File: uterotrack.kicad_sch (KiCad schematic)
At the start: 0 parts

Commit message: Add schematics
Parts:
- added AE?: Antenna_Shield, myDevices:SMD_PAD_4x1.5mm, symbol Device:Antenna
- added C? (x2): C, Capacitor_SMD:C_0402_1005Metric, symbol Device:C
- added C? (x5): 100nF, Capacitor_SMD:C_0603_1608Metric, symbol Device:C
- added C? (x2): 10uF, Capacitor_SMD:C_0603_1608Metric, symbol Device:C
- added C?: 1uF, Capacitor_SMD:C_0603_1608Metric, symbol Device:C
- added C?: 10nF, Capacitor_SMD:C_0603_1608Metric, symbol Device:C
- added D?: QLS6B-FKW, LED_SMD:LED_Cree-PLCC6_4.7x1.5mm, symbol LED:QLS6B-FKW
- added J?: RFShield, myDevices:Wuerth_36103255S_25x25mm, symbol Device:RFShield_OnePiece
- added J?: Argos_Prog, Connector_Molex:Molex_PicoBlade_53047-0510_1x05_P1.25mm_Vertical, symbol Connector_Generic:Conn_01x05
- added J?: MicroSD_Card, myDevices:microSD, symbol myDevices:Micro_SD_Card
- added J?: EXP, Connector_PinHeader_2.54mm:PinHeader_1x02_P2.54mm_Vertical, symbol Connector_Generic:Conn_01x02
- added J?: Prog, Connector_Molex:Molex_PicoBlade_53047-0510_1x05_P1.25mm_Vertical, symbol Connector_Generic:Conn_01x05
- added JP?: SolderJumper_3_Open, Jumper:SolderJumper-3_P1.3mm_Open_RoundedPad1.0x1.5mm, symbol Jumper:SolderJumper_3_Open
- added L?: L, Inductor_SMD:L_0603_1608Metric, symbol Device:L
- added Q? (x3): MMBT2222, Package_TO_SOT_SMD:SOT-323_SC-70, symbol Transistor_BJT:Q_NPN_BEC
- added Q?: SiS415DNT, Package_SO:Vishay_PowerPAK_1212-8_Single, symbol Transistor_FET:SiS415DNT
- added Q? (x4): SI2305, Package_TO_SOT_SMD:SOT-23, symbol Transistor_FET:Q_PMOS_GSD
- added Q? (x3): MMBT2222, Package_TO_SOT_SMD:SOT-23, symbol Transistor_BJT:Q_NPN_BEC
- added R? (x9): 10k, Resistor_SMD:R_0603_1608Metric, symbol Device:R
- added R? (x12): 100k, Resistor_SMD:R_0603_1608Metric, symbol Device:R
- added R? (x2): 20k, Resistor_SMD:R_0603_1608Metric, symbol Device:R
- added R? (x6): 0R, Resistor_SMD:R_0603_1608Metric, symbol Device:R
- added R? (x3): 4k7, Resistor_SMD:R_0603_1608Metric, symbol Device:R
- added RN? (x4): 470R, Resistor_SMD:R_Array_Convex_4x0603, symbol Device:R_Pack04_Split
- added U?: RV-3032-C7, myDevices:RTC_SMD_MicroCrystal_C7_1.5x3.2mm, symbol myDevices:RV-3032-C7
- added U?: Argos_SMD, myDevices:Argos-SMD_shortLegs, symbol myDevices:Argos_SMD
- added U?: ESP32-S3-WROOM-1, RF_Module:ESP32-S3-WROOM-1, symbol myDevices:ESP32-S3-WROOM-1
- added U?: CAM-M8Q, myDevices:ublox_CAM-M8, symbol myDevices:CAM-M8Q
- added U?: keller_6LHPD, myDevices:keller_6LD, symbol myDevices:keller_6LHPD
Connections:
- new net: Q?.1 (B), R?.2 (x6)
- new net: Q?.3 (C), RN?.1 (R1.1) (x3)
- new net: R?.1, U?.1 (VBACKUP)
- new net: JP?.2 (C), U?.30 (V_{BAT})
- new net: Q?.1 (G), Q?.3 (C), R?.2 (x2)
- new net: C?.1, Q?.3 (D), U?.1 (VCC_IO), U?.9 (VCC)
- new net: J?.7 (DAT0), R?.1, R?.2
- new net: C?.2, J?.4 (VDD), Q?.3 (D), R?.2, R?.2, R?.2, R?.2, R?.2, R?.2
- new net: Q?.3 (C), Q?.4 (G), R?.2
- new net: J?.2 (Pin_2), Q?.5 (D)
- new net: D?.2 (KB), RN?.8 (R1.2)
- new net: J?.5 (CLK), R?.1, R?.2
- new net: Q?.3 (D), R?.1
- new net: J?.1 (DAT2), R?.1, R?.2
- new net: J?.2 (DAT3/CD), R?.1, R?.2
- new net: J?.8 (DAT1), R?.1, R?.2
- new net: J?.3 (CMD), R?.1, R?.2
- new net: D?.4 (KR), RN?.8 (R1.2), RN?.8 (R1.2)
- new net: U?.16 (RF_OUT), U?.17 (RF_IN)
- new net: D?.6 (KR), RN?.8 (R1.2)
- new net 3V3: C?.1, C?.1, C?.2, C?.2, J?.5 (Pin_5), Q?.2 (S), Q?.2 (S), Q?.2 (S), R?.1, R?.1, R?.1, R?.1, R?.1, R?.2, R?.2, R?.2, U?.2 (3V3), U?.3 (SUP)
- new net ADC: R?.1, R?.2, U?.15 (IO3)
- new net ADC_EN: R?.1, U?.14 (IO20)
- new net ANT_1: C?.1, L?.1, U?.18 (ANT)
- new net ANT_2: AE?.1 (A), C?.1, L?.2
- new net APA_3V3: U?.7 (VDD_PA), U?.8 (VDD_PA)
- new net APA_EN: U?.9 (PA_EN)
- new net APA_SEL: U?.10 (PA_PGOOD)
- new net ARG_RST: J?.2 (Pin_2), U?.35 (~{RST})
- new net ARG_SWDCLK: J?.4 (Pin_4), U?.25 (SWCLK)
- new net ARG_SWDIO: J?.3 (Pin_3), U?.26 (SWDIO)
- new net Argos_EN: R?.1, U?.12 (IO8)
- new net Argos_RxD: U?.4 (LP_RX), U?.8 (IO15)
- new net Argos_TxD: U?.5 (LP_TX), U?.9 (IO16)
- new net Argus_3V3: C?.1, JP?.1 (A), Q?.3 (D), U?.31 (VDD), U?.32 (VDD)
- new net BOut: Q?.2 (S), R?.1
- new net Batt: C?.1, D?.1 (AB), D?.3 (AR), D?.5 (AG), Q?.1 (S), Q?.2 (S), Q?.3 (S), R?.1, U?.6 (VDD)
- new net Blue: R?.1, U?.39 (IO1)
- new net Charge: RN?.1 (R1.1)
- new net EXP_EN: R?.1, R?.1, U?.30 (IO37)
- new net GND: C?.1, C?.1, C?.1, C?.2, C?.2, C?.2, C?.2, C?.2, C?.2, C?.2, C?.2, J?.1 (Pin_1), J?.1 (Pin_1), J?.1 (Pin_1), J?.1 (Shield), J?.6 (VSS), Q?.2 (E), Q?.2 (E), Q?.2 (E), Q?.2 (E), Q?.2 (E), Q?.2 (E), R?.2, R?.2, R?.2, U?.1 (GND), U?.1 (GND), U?.10 (GND), U?.11 (GND), U?.12 (GND), U?.13 (GND), U?.13 (GND), U?.14 (GND), U?.14 (GND), U?.15 (GND), U?.15 (GND), U?.16 (GND), U?.17 (GND), U?.18 (GND), U?.19 (GND), U?.19 (GND), U?.20 (GND), U?.21 (GND), U?.21 (GND), U?.22 (GND), U?.27 (GND), U?.29 (GND), U?.31 (GND), U?.4 (GND), U?.40 (GND), U?.41 (EPAD), U?.5 (GND), U?.5 (VSS), U?.6 (GND)
- new net GNSS_EN: Q?.1 (G), R?.2, U?.7 (IO7)
- new net Green: R?.1, U?.38 (IO2)
- new net Hal_ST: U?.31 (IO38)
- new net I2C1_SCL: R?.2, U?.2 (SCL), U?.29 (IO36), U?.8 (SCL)
- new net I2C1_SDA: R?.1, U?.2 (SDA), U?.28 (IO35), U?.4 (SDA)
- new net I2C2_SCL: U?.23 (IO21)
- new net I2C2_SDA: U?.25 (IO48)
- new net IO0: J?.5 (Pin_5), R?.2, U?.27 (IO0)
- new net Main: U?.32 (IO39)
- new net Ox_EN: U?.26 (IO45)
- new net Ox_RxD1: U?.5 (IO5)
- new net Ox_TxD1: U?.6 (IO6)
- new net Prog_RxD: J?.2 (Pin_2), U?.36 (RXD0/IO44)
- new net Prog_TxD: J?.3 (Pin_3), U?.37 (TXD0/IO43)
- new net RST: C?.1, J?.4 (Pin_4), R?.1, U?.3 (EN)
- new net RTC_INT: R?.1, U?.3 (~{INT}), U?.33 (IO40)
- new net Red: R?.1, U?.4 (IO4)
- new net S3_GNSS_RxD: U?.10 (IO17), U?.25 (TXD/SPI_MISO)
- new net S3_GNSS_TxD: U?.11 (IO18), U?.26 (RXD/SPI_MOSI)
- new net SDIO_CLK: R?.1, U?.19 (IO11)
- new net SDIO_CMD: R?.1, U?.20 (IO12)
- new net SDIO_D0: R?.1, U?.18 (IO10)
- new net SDIO_D1: R?.1, U?.17 (IO9)
- new net SDIO_D2: R?.1, U?.22 (IO14)
- new net SDIO_D3: R?.1, U?.21 (IO13)
- new net VBackup: JP?.3 (B), U?.8 (V_BCKP)
- new net keller_EOC: U?.16 (IO46), U?.5 (EOC)
- new net uCard_EN: Q?.1 (G), R?.2, U?.24 (IO47)
- no-connect marks 0 -> 26
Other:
- added sheet power (power.kicad_sch)
- note added: "ESP32-S3: - Use any module without PSRAM - With PSRAM needs testeing - Incompatible With PSRAM Octal SPI, pins already in use"
- note added: "MMBT2222AWT3G"
- company: (none) -> ElectricBlue
- title: (none) -> Trident V3

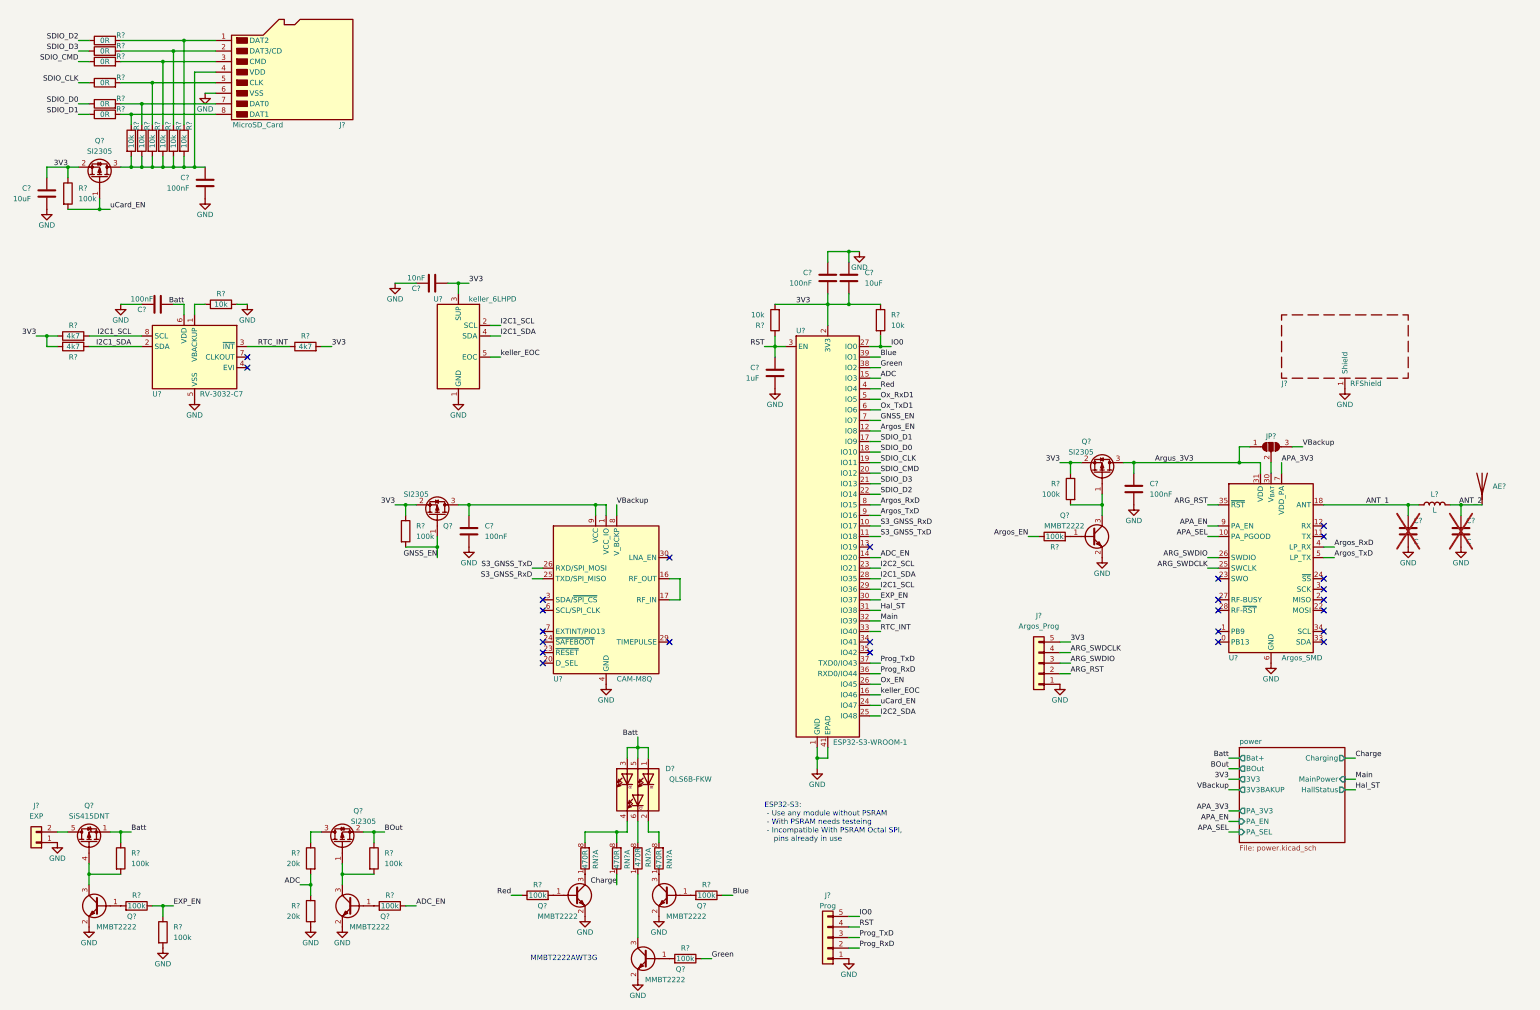
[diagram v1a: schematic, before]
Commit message: Add AS5510 as external sensor, update ESP32 IO
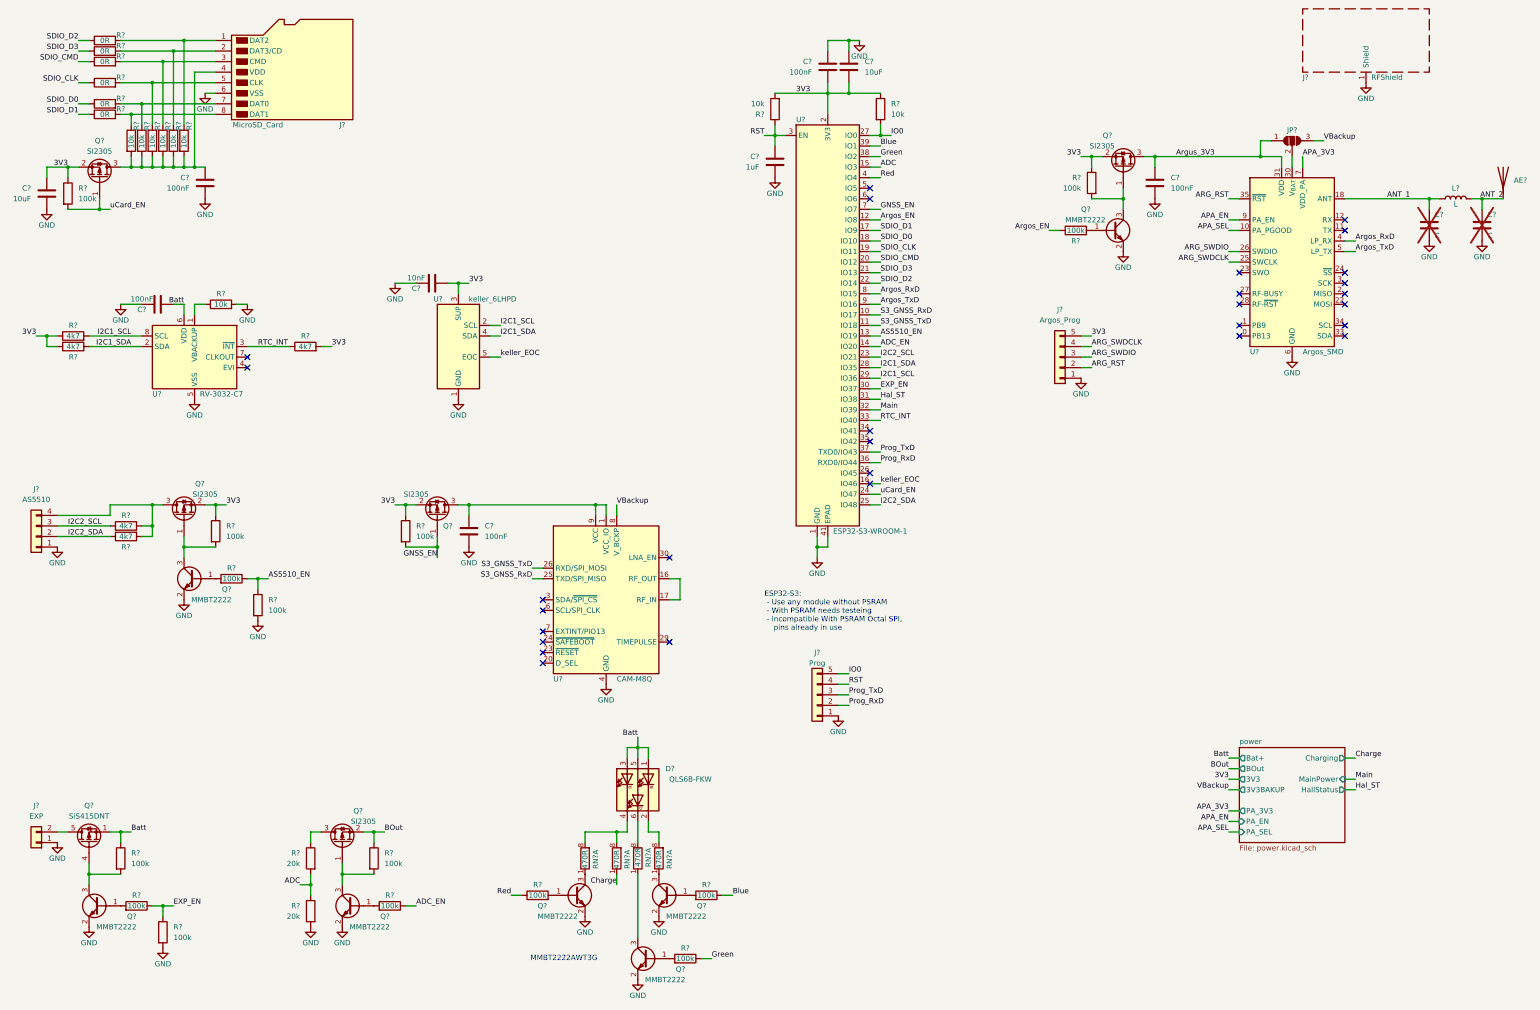
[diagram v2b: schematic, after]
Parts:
- added J?: AS5510, Connector_Molex:Molex_PicoBlade_53048-0410_1x04_P1.25mm_Horizontal, symbol Connector_Generic:Conn_01x04
- added Q?: SI2305, Package_TO_SOT_SMD:SOT-23, symbol Transistor_FET:Q_PMOS_GSD
- added Q?: MMBT2222, Package_TO_SOT_SMD:SOT-23, symbol Transistor_BJT:Q_NPN_BEC
- added R? (x3): 100k, Resistor_SMD:R_0603_1608Metric, symbol Device:R
- added R? (x2): 4k7, Resistor_SMD:R_0603_1608Metric, symbol Device:R
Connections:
- net 3V3: now also Q?.2 (S), R?.1
- net GND: now also J?.1 (Pin_1), Q?.2 (E), R?.2
- net I2C2_SCL: now also J?.3 (Pin_3), R?.2
- net I2C2_SDA: now also J?.2 (Pin_2), R?.1
- net AS5510_EN: now reaches U?.13 (IO19)
- net AS5510_EN: now also R?.1, R?.1
- net Ox_EN: no longer names the net of U?.26 (IO45)
- net Ox_RxD1: no longer names the net of U?.5 (IO5)
- net Ox_TxD1: no longer names the net of U?.6 (IO6)
- new net: Q?.1 (B), R?.2
- new net: Q?.1 (G), Q?.3 (C), R?.2
- new net: J?.4 (Pin_4), Q?.3 (D), R?.1, R?.2
- no-connect marks 26 -> 29
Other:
- moved on the sheet: AE?, C?, J?, JP?, L?, Q?, R?, U?

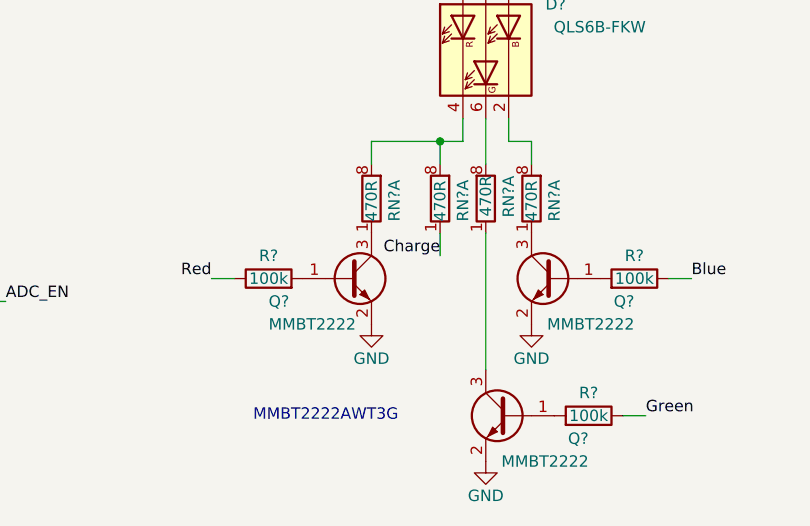
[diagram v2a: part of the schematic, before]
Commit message: Fix led circuit
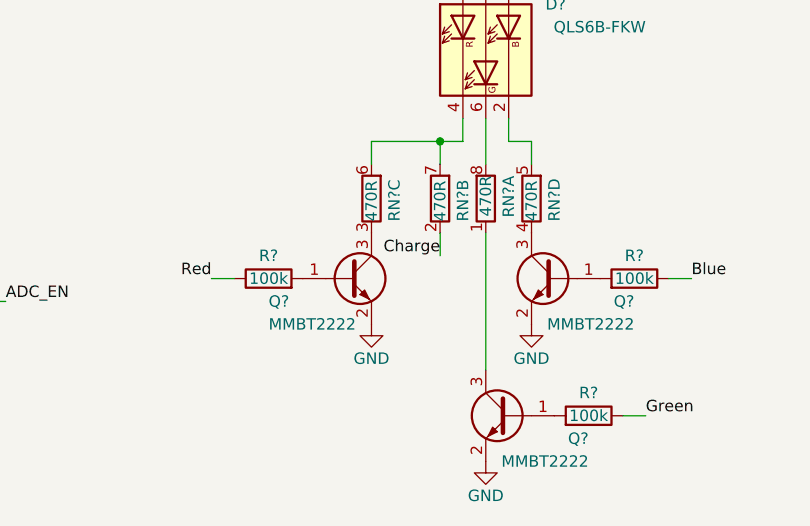
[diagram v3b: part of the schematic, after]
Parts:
- Q? (x3): footprint Package_TO_SOT_SMD:SOT-323_SC-70 -> Package_TO_SOT_SMD:SOT-23; manf# MMBT2222AWT3G -> MMBT2222ALT3G
- RN? (x4): footprint Resistor_SMD:R_Array_Convex_4x0603 -> myDevices:R_Array_Convex_Panasonic_EXB38V_4x0603
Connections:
- net Charge: now also RN?.2 (R2.1); no longer RN?.1 (R1.1)
- net at Q?.3 (C): now also RN?.3 (R3.1); no longer RN?.1 (R1.1)
- net at Q?.3 (C): now also RN?.4 (R4.1); no longer RN?.1 (R1.1)
- net at D?.2 (KB): now also RN?.5 (R4.2); no longer RN?.8 (R1.2)
- new net: D?.4 (KR), RN?.6 (R3.2), RN?.7 (R2.2)
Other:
- note removed: "MMBT2222AWT3G"
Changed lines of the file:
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@@
 		)
 	)
-	(text "MMBT2222AWT3G"
-		(exclude_from_sim no)
-		(at 167.64 259.08 0)
-		(effects
-			(font
-				(size 1.27 1.27)
-			)
-		)
-	)
 	(junction
 		(at 66.04 53.34)
@@
 			)
 		)
-		(property "Footprint" "Package_TO_SOT_SMD:SOT-323_SC-70"
+		(property "Footprint" "Package_TO_SOT_SMD:SOT-23"
 			(at 182.88 256.54 0)
 			(effects
@@
 			)
 		)
-		(property "manf#" "MMBT2222AWT3G"
+		(property "manf#" "MMBT2222ALT3G"
 			(at 187.96 259.08 0)
 			(effects
@@
 			)
 		)
-		(property "Footprint" "Package_TO_SOT_SMD:SOT-323_SC-70"
+		(property "Footprint" "Package_TO_SOT_SMD:SOT-23"
 			(at 175.26 241.3 0)
 			(effects
@@
 			)
 		)
-		(property "manf#" "MMBT2222AWT3G"
+		(property "manf#" "MMBT2222ALT3G"
 			(at 170.18 243.84 0)
 			(effects
@@
 		(lib_id "Device:R_Pack04_Split")
 		(at 190.5 234.95 0)
-		(unit 1)
+		(unit 4)
 		(exclude_from_sim no)
 		(in_bom yes)
@@
 			)
 		)
-		(property "Footprint" "Resistor_SMD:R_Array_Convex_4x0603"
+		(property "Footprint" "myDevices:R_Array_Convex_Panasonic_EXB38V_4x0603"
 			(at 188.468 234.95 90)
 			(effects
@@
 				(path "/02cd0949-8d8d-4522-9baa-94804311f80f"
 					(reference "RN?")
-					(unit 1)
+					(unit 4)
 				)
 			)
@@
 		(lib_id "Device:R_Pack04_Split")
 		(at 180.34 234.95 0)
-		(unit 1)
+		(unit 2)
 		(exclude_from_sim no)
 		(in_bom yes)
@@
 			)
 		)
-		(property "Footprint" "Resistor_SMD:R_Array_Convex_4x0603"
+		(property "Footprint" "myDevices:R_Array_Convex_Panasonic_EXB38V_4x0603"
 			(at 178.308 234.95 90)
 			(effects
@@
 				(path "/02cd0949-8d8d-4522-9baa-94804311f80f"
 					(reference "RN?")
-					(unit 1)
+					(unit 2)
 				)
 			)
@@
 			)
 		)
-		(property "Footprint" "Resistor_SMD:R_Array_Convex_4x0603"
+		(property "Footprint" "myDevices:R_Array_Convex_Panasonic_EXB38V_4x0603"
 			(at 187.452 234.95 90)
 			(effects
@@
 			)
 		)
-		(property "Footprint" "Package_TO_SOT_SMD:SOT-323_SC-70"
+		(property "Footprint" "Package_TO_SOT_SMD:SOT-23"
 			(at 187.96 241.3 0)
 			(effects
@@
 			)
 		)
-		(property "manf#" "MMBT2222AWT3G"
+		(property "manf#" "MMBT2222ALT3G"
 			(at 193.04 243.84 0)
 			(effects
@@
 		(lib_id "Device:R_Pack04_Split")
 		(at 172.72 234.95 0)
-		(unit 1)
+		(unit 3)
 		(exclude_from_sim no)
 		(in_bom yes)
@@
 			)
 		)
-		(property "Footprint" "Resistor_SMD:R_Array_Convex_4x0603"
+		(property "Footprint" "myDevices:R_Array_Convex_Panasonic_EXB38V_4x0603"
 			(at 170.688 234.95 90)
 			(effects
@@
 				(path "/02cd0949-8d8d-4522-9baa-94804311f80f"
 					(reference "RN?")
-					(unit 1)
+					(unit 3)
 				)
 			)
